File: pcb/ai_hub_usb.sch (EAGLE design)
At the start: 31 parts, among them IC1 FE1.1S

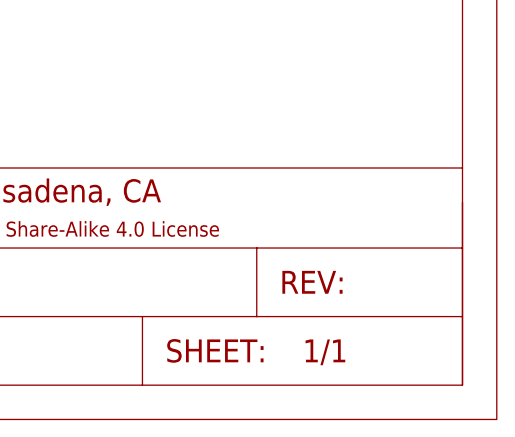
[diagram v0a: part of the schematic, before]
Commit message: updating LED spacing
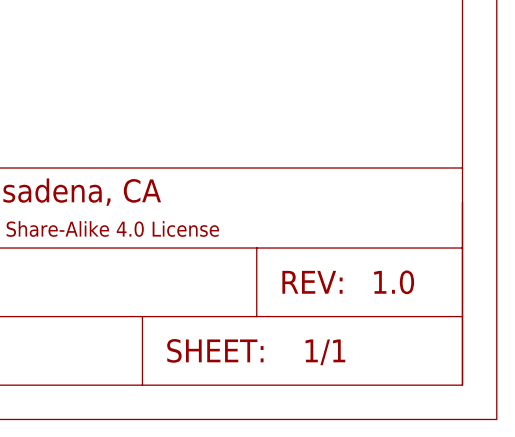
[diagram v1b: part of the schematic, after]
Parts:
- FRAME1: REV (none) -> 1.0
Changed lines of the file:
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@@
 </classes>
 <parts>
-<part name="FRAME1" library="Ai_Miscellany" deviceset="FRAME-LETTER" device=""/>
+<part name="FRAME1" library="Ai_Miscellany" deviceset="FRAME-LETTER" device="">
+<attribute name="REV" value="1.0"/>
+</part>
 <part name="IC1" library="Ai_IC" deviceset="FE1.1S" device=""/>
 <part name="GND1" library="Ai_Power" deviceset="GND" device=""/>
